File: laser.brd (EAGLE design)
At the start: 74.9 x 82.5 mm, 26 parts

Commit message: Routing checked, first test
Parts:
- removed NPN: (no value), SparkFun-DiscreteSemi:TO-92
- added 2N2222: (no value), SparkFun-DiscreteSemi:TO-92
- moved END_X 7.62 mm to (58.4, 6.35), turned to 180 degrees
- moved END_Y 7.62 mm to (66.0, 6.35), turned to 0 degrees
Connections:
- net GND: now also 2N2222.1; no longer NPN.3
- net S$20: now also 2N2222.2; no longer NPN.2
- net S$21: now also 2N2222.3; no longer NPN.1
- net S$23: now also END_X.1; no longer END_Y.1
- net S$24: now also END_Y.1; no longer END_X.1
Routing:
- net S$21: track 31.3 -> 33.7 mm
- net GND: track 239.2 -> 237.7 mm
- net S$20: track 4.97 -> 6.24 mm
- net S$3: track 147.3 -> 148.3 mm
- removed copper zone on layer 16, net 5V
- removed copper zone on layer 16, net S$25
- removed copper zone on layer 16, net S$28
- removed copper zone on layer 16, net S$30
- removed copper zone on layer 16, net S$31
- removed copper zone on layer 16, net S$32
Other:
- board text removed: "青"

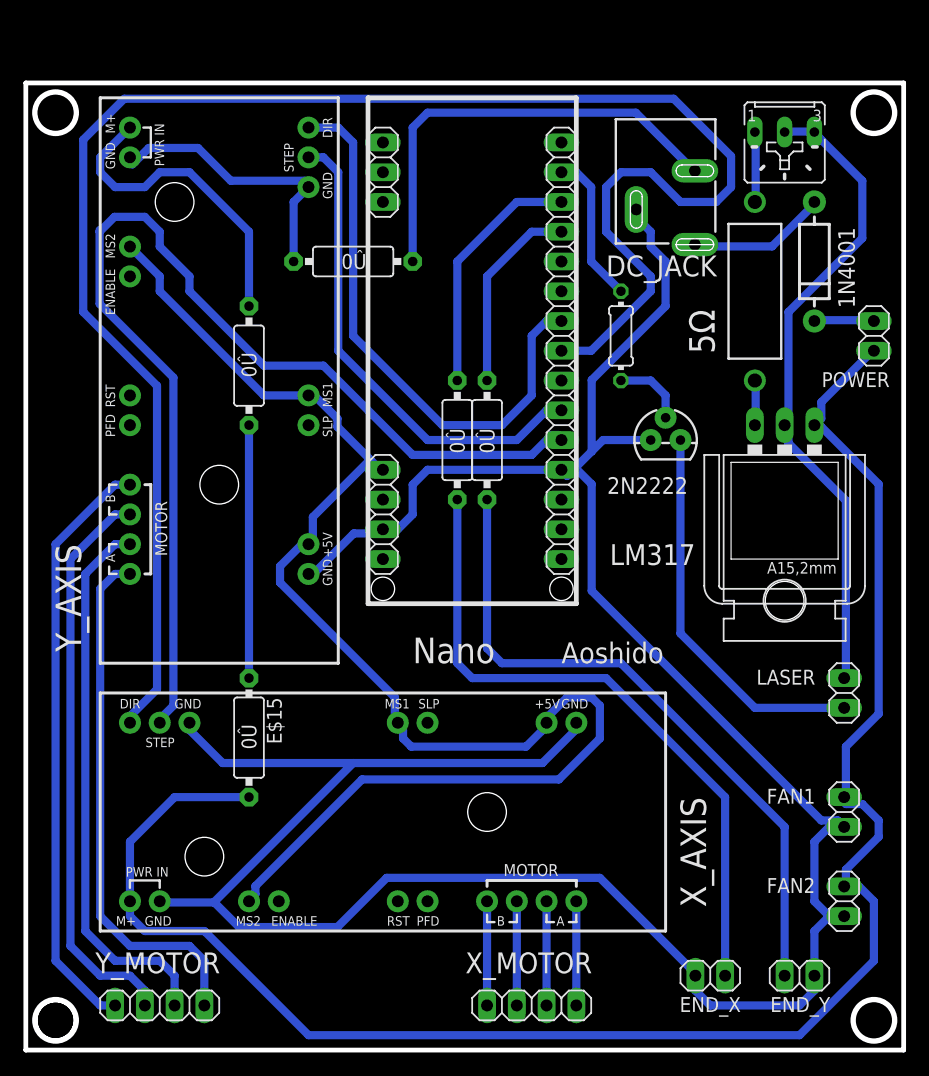
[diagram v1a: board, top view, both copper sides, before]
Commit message: New design, exporting laser driver
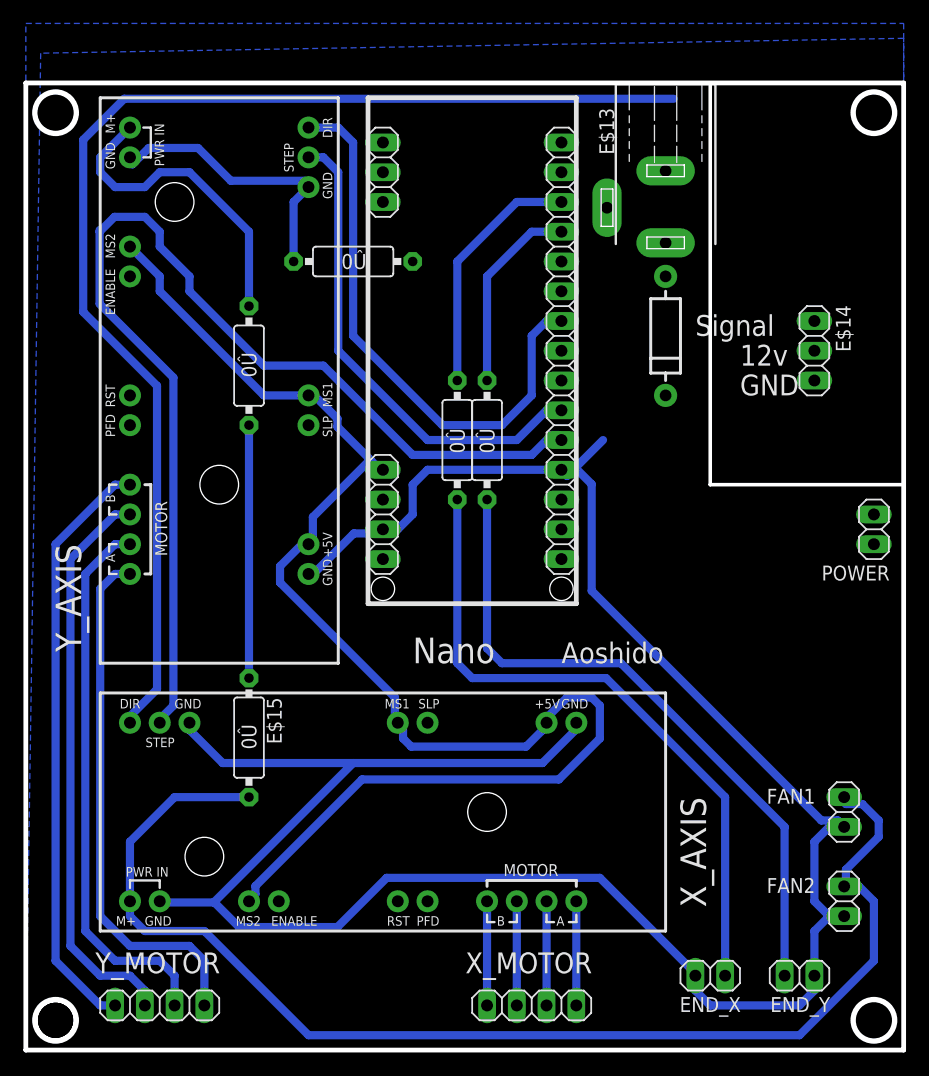
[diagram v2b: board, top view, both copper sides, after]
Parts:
- removed 2N2222: (no value), SparkFun-DiscreteSemi:TO-92
- removed DC_JACK: (no value), SparkFun-Connectors:POWER_JACK_SLOT
- removed E$1: (no value), heatsink:D01S
- removed E$4: 5Ω, SparkFun-Resistors:AXIAL-0.6
- removed E$6: 50Ω, pot:B25U
- removed E$9: 220Ω, eagle-ltspice:0204/7
- removed LASER: (no value), pinhead:1X02
- removed LM317: (no value), v-reg:78XXL
- added E$13: (no value), con-conrad:733980-62
- added E$14: (no value), pinhead:1X03
- moved POWER 16.5 mm to (72.4, 44.5)
- moved E$8 14.2 mm to (54.6, 61.0)
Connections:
- removed net S$16: E$4.P$2, LM317.OUT
- removed net S$18: E$4.P$1, E$6.A
- removed net S$20: 2N2222.2, E$9.2
- removed net S$21: 2N2222.3, LASER.1
- removed net S$28: DC_JACK.GND@1, E$12.1
- removed net S$5: E$6.E, E$6.S, LASER.2, LM317.GND
- net 12V: now also E$14.2; no longer LM317.IN
- net GND: now also E$12.1, E$13.2, E$13.3, E$14.3; no longer 2N2222.1, DC_JACK.GND@2
- net S$19: now also E$13.1; no longer DC_JACK.PWR
- net S$6: now also E$14.1; no longer E$9.1
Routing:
- net S$5: track 55.8 -> 0.00 mm
- net 12V: track 151.5 -> 107.5 mm
- net S$3: track 148.3 -> 105.8 mm
- net S$28: track 38.5 -> 0.00 mm
- net S$21: track 33.7 -> 0.00 mm
- net GND: track 237.7 -> 209.3 mm
- net S$6: track 13.0 -> 0.00 mm
- net S$19: track 11.9 -> 0.00 mm
- net S$20: track 6.24 -> 0.00 mm
- net S$18: track 5.98 -> 0.00 mm
- net S$22: track 5.09 -> 0.00 mm
- net S$16: track 3.82 -> 0.00 mm
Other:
- outline, holes or cut-outs redrawn
- board text added: "12v"
- board text added: "GND"
- board text added: "Signal"
